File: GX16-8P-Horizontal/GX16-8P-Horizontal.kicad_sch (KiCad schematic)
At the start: 2 parts, among them J1 GX16, J2 Board Header

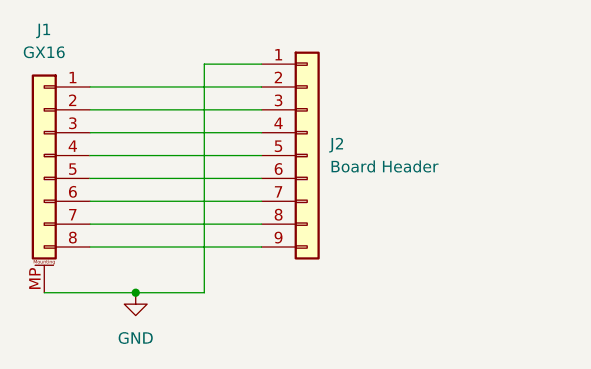
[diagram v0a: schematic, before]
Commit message: https://github.com/Halibut-Electronics/HHI-Radio-Pro/issues/34 Switched from pins to card edge.
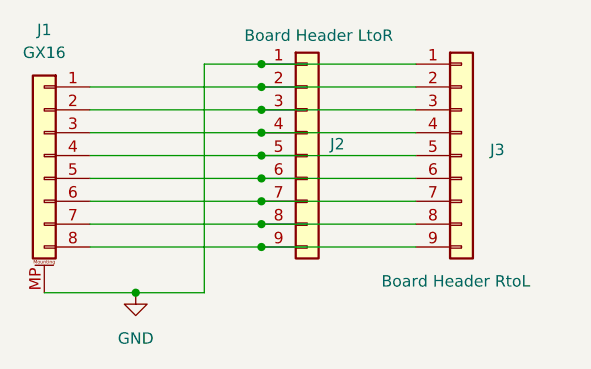
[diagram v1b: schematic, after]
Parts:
- added J3: Board Header RtoL, Libraries:Conn_B2B-RA_2.54mm_ThroughPads_9pin_RtoL, symbol Connector_Generic:Conn_01x09
- J2: value Board Header -> Board Header LtoR; footprint Connector_PinHeader_2.54mm:PinHeader_1x09_P2.54mm_Vertical -> Libraries:Conn_B2B-RA_2.54mm_ThroughPads_9pin_LtoR
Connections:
- net GND: now also J3.1 (Pin_1)
- net at J1.1 (Pin_1), J2.2 (Pin_2): now also J3.2 (Pin_2)
- net at J1.2 (Pin_2), J2.3 (Pin_3): now also J3.3 (Pin_3)
- net at J1.3 (Pin_3), J2.4 (Pin_4): now also J3.4 (Pin_4)
- net at J1.4 (Pin_4), J2.5 (Pin_5): now also J3.5 (Pin_5)
- net at J1.5 (Pin_5), J2.6 (Pin_6): now also J3.6 (Pin_6)
- net at J1.6 (Pin_6), J2.7 (Pin_7): now also J3.7 (Pin_7)
- net at J1.7 (Pin_7), J2.8 (Pin_8): now also J3.8 (Pin_8)
- net at J1.8 (Pin_8), J2.9 (Pin_9): now also J3.9 (Pin_9)
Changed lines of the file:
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@@
-(kicad_sch (version 20211123) (generator eeschema)
+(kicad_sch (version 20230121) (generator eeschema)
   (paper "A4")
+  (junction (at 127 76.2) (diameter 0) (color 0 0 0 0)
+  )
+  (junction (at 127 73.66) (diameter 0) (color 0 0 0 0)
+  )
+  (junction (at 127 83.82) (diameter 0) (color 0 0 0 0)
+  )
+  (junction (at 127 86.36) (diameter 0) (color 0 0 0 0)
+  )
+  (junction (at 127 91.44) (diameter 0) (color 0 0 0 0)
+  )
   (junction (at 113.03 99.06) (diameter 0) (color 0 0 0 0)
   )
+  (junction (at 127 88.9) (diameter 0) (color 0 0 0 0)
+  )
+  (junction (at 127 78.74) (diameter 0) (color 0 0 0 0)
+  )
+  (junction (at 127 93.98) (diameter 0) (color 0 0 0 0)
+  )
+  (junction (at 127 81.28) (diameter 0) (color 0 0 0 0)
+  )
+  (wire (pts (xy 127 91.44) (xy 144.145 91.44))
+    (stroke (width 0) (type default))
+  )
   (wire (pts (xy 107.95 91.44) (xy 127 91.44))
-    (stroke (width 0) (type default) (color 0 0 0 0))
+    (stroke (width 0) (type default))
   )
   (wire (pts (xy 120.65 73.66) (xy 127 73.66))
-    (stroke (width 0) (type default) (color 0 0 0 0))
+    (stroke (width 0) (type default))
   )
   (wire (pts (xy 107.95 86.36) (xy 127 86.36))
-    (stroke (width 0) (type default) (color 0 0 0 0))
+    (stroke (width 0) (type default))
   )
   (wire (pts (xy 113.03 99.06) (xy 120.65 99.06))
-    (stroke (width 0) (type default) (color 0 0 0 0))
+    (stroke (width 0) (type default))
+  )
+  (wire (pts (xy 127 81.28) (xy 144.145 81.28))
+    (stroke (width 0) (type default))
   )
   (wire (pts (xy 107.95 93.98) (xy 127 93.98))
-    (stroke (width 0) (type default) (color 0 0 0 0))
+    (stroke (width 0) (type default))
   )
   (wire (pts (xy 107.95 83.82) (xy 127 83.82))
-    (stroke (width 0) (type default) (color 0 0 0 0))
+    (stroke (width 0) (type default))
+  )
+  (wire (pts (xy 127 93.98) (xy 144.145 93.98))
+    (stroke (width 0) (type default))
+  )
+  (wire (pts (xy 127 78.74) (xy 144.145 78.74))
+    (stroke (width 0) (type default))
   )
   (wire (pts (xy 107.95 78.74) (xy 127 78.74))
-    (stroke (width 0) (type default) (color 0 0 0 0))
+    (stroke (width 0) (type default))
   )
   (wire (pts (xy 102.87 99.06) (xy 113.03 99.06))
-    (stroke (width 0) (type default) (color 0 0 0 0))
+    (stroke (width 0) (type default))
+  )
+  (wire (pts (xy 127 83.82) (xy 144.145 83.82))
+    (stroke (width 0) (type default))
+  )
+  (wire (pts (xy 127 86.36) (xy 144.145 86.36))
+    (stroke (width 0) (type default))
+  )
+  (wire (pts (xy 127 73.66) (xy 144.145 73.66))
+    (stroke (width 0) (type default))
   )
   (wire (pts (xy 107.95 88.9) (xy 127 88.9))
-    (stroke (width 0) (type default) (color 0 0 0 0))
+    (stroke (width 0) (type default))
   )
   (wire (pts (xy 107.95 81.28) (xy 127 81.28))
-    (stroke (width 0) (type default) (color 0 0 0 0))
+    (stroke (width 0) (type default))
   )
   (wire (pts (xy 107.95 76.2) (xy 127 76.2))
-    (stroke (width 0) (type default) (color 0 0 0 0))
+    (stroke (width 0) (type default))
   )
   (wire (pts (xy 120.65 99.06) (xy 120.65 73.66))
-    (stroke (width 0) (type default) (color 0 0 0 0))
+    (stroke (width 0) (type default))
+  )
+  (wire (pts (xy 127 76.2) (xy 144.145 76.2))
+    (stroke (width 0) (type default))
+  )
+  (wire (pts (xy 127 88.9) (xy 144.145 88.9))
+    (stroke (width 0) (type default))
   )
   (symbol (lib_id "Connector_Generic_MountingPin:Conn_01x08_MountingPin") (at 102.87 83.82 0) (mirror y) (unit 1)
-    (in_bom yes) (on_board yes) (fields_autoplaced)
-    (property "Reference" "J1" (id 0) (at 102.87 69.85 0))
-    (property "Value" "GX16" (id 1) (at 102.87 72.39 0))
-    (property "Footprint" "Libraries:Conn_GX16-8_8pin_Aviation" (id 2) (at 102.87 83.82 0)
-      (effects (font (size 1.27 1.27)) hide)
-    )
-    (property "Datasheet" "~" (id 3) (at 102.87 83.82 0)
+    (in_bom yes) (on_board yes) (dnp no) (fields_autoplaced)
+    (property "Reference" "J1" (at 102.87 69.85 0)
+      (effects (font (size 1.27 1.27)))
+    )
+    (property "Value" "GX16" (at 102.87 72.39 0)
+      (effects (font (size 1.27 1.27)))
+    )
+    (property "Footprint" "Libraries:Conn_GX16-8_8pin_Aviation" (at 102.87 83.82 0)
+      (effects (font (size 1.27 1.27)) hide)
+    )
+    (property "Datasheet" "~" (at 102.87 83.82 0)
       (effects (font (size 1.27 1.27)) hide)
     )
@@
     (pin "8")
     (pin "MP")
+    (instances
+      (project "GX16-8P-Horizontal"
+        (path "/40766177-b422-41a1-81e1-f70193c63cbd"
+          (reference "J1") (unit 1)
+        )
+      )
+    )
   )
   (symbol (lib_id "power:GND") (at 113.03 99.06 0) (unit 1)
-    (in_bom yes) (on_board yes) (fields_autoplaced)
-    (property "Reference" "#PWR01" (id 0) (at 113.03 105.41 0)
-      (effects (font (size 1.27 1.27)) hide)
-    )
-    (property "Value" "GND" (id 1) (at 113.03 104.14 0))
-    (property "Footprint" "" (id 2) (at 113.03 99.06 0)
-      (effects (font (size 1.27 1.27)) hide)
-    )
-    (property "Datasheet" "" (id 3) (at 113.03 99.06 0)
-      (effects (font (size 1.27 1.27)) hide)
-    )
-    (pin "1")
-  )
-  (symbol (lib_id "Connector_Generic:Conn_01x09") (at 132.08 83.82 0) (unit 1)
-    (in_bom yes) (on_board yes) (fields_autoplaced)
-    (property "Reference" "J2" (id 0) (at 134.62 82.5499 0)
-      (effects (font (size 1.27 1.27)) (justify left))
-    )
-    (property "Value" "Board Header" (id 1) (at 134.62 85.0899 0)
-      (effects (font (size 1.27 1.27)) (justify left))
-    )
-    (property "Footprint" "Connector_PinHeader_2.54mm:PinHeader_1x09_P2.54mm_Vertical" (id 2) (at 132.08 83.82 0)
-      (effects (font (size 1.27 1.27)) hide)
-    )
-    (property "Datasheet" "~" (id 3) (at 132.08 83.82 0)
+    (in_bom yes) (on_board yes) (dnp no) (fields_autoplaced)
+    (property "Reference" "#PWR01" (at 113.03 105.41 0)
+      (effects (font (size 1.27 1.27)) hide)
+    )
+    (property "Value" "GND" (at 113.03 104.14 0)
+      (effects (font (size 1.27 1.27)))
+    )
+    (property "Footprint" "" (at 113.03 99.06 0)
+      (effects (font (size 1.27 1.27)) hide)
+    )
+    (property "Datasheet" "" (at 113.03 99.06 0)
+      (effects (font (size 1.27 1.27)) hide)
+    )
+    (pin "1")
+    (instances
+      (project "GX16-8P-Horizontal"
+        (path "/40766177-b422-41a1-81e1-f70193c63cbd"
+          (reference "#PWR01") (unit 1)
+        )
+      )
+    )
+  )
+  (symbol (lib_id "Connector_Generic:Conn_01x09") (at 149.225 83.82 0) (unit 1)
+    (in_bom yes) (on_board yes) (dnp no)
+    (property "Reference" "J3" (at 152.4 83.185 0)
+      (effects (font (size 1.27 1.27)) (justify left))
+    )
+    (property "Value" "Board Header RtoL" (at 140.335 97.79 0)
+      (effects (font (size 1.27 1.27)) (justify left))
+    )
+    (property "Footprint" "Libraries:Conn_B2B-RA_2.54mm_ThroughPads_9pin_RtoL" (at 149.225 83.82 0)
+      (effects (font (size 1.27 1.27)) hide)
+    )
+    (property "Datasheet" "~" (at 149.225 83.82 0)
       (effects (font (size 1.27 1.27)) hide)
     )
@@
     (pin "8")
     (pin "9")
+    (instances
+      (project "GX16-8P-Horizontal"
+        (path "/40766177-b422-41a1-81e1-f70193c63cbd"
+          (reference "J3") (unit 1)
+        )
+      )
+    )
+  )
+  (symbol (lib_id "Connector_Generic:Conn_01x09") (at 132.08 83.82 0) (unit 1)
+    (in_bom yes) (on_board yes) (dnp no)
+    (property "Reference" "J2" (at 134.62 82.5499 0)
+      (effects (font (size 1.27 1.27)) (justify left))
+    )
+    (property "Value" "Board Header LtoR" (at 125.095 70.485 0)
+      (effects (font (size 1.27 1.27)) (justify left))
+    )
+    (property "Footprint" "Libraries:Conn_B2B-RA_2.54mm_ThroughPads_9pin_LtoR" (at 132.08 83.82 0)
+      (effects (font (size 1.27 1.27)) hide)
+    )
+    (property "Datasheet" "~" (at 132.08 83.82 0)
+      (effects (font (size 1.27 1.27)) hide)
+    )
+    (pin "1")
+    (pin "2")
+    (pin "3")
+    (pin "4")
+    (pin "5")
+    (pin "6")
+    (pin "7")
+    (pin "8")
+    (pin "9")
+    (instances
+      (project "GX16-8P-Horizontal"
+        (path "/40766177-b422-41a1-81e1-f70193c63cbd"
+          (reference "J2") (unit 1)
+        )
+      )
+    )
   )
   (sheet_instances
     (path "/" (page "1"))
   )
-  (symbol_instances
-    (path "/6b0d7141-ab3f-4a87-a24b-a2c211da2bd1"
-      (reference "#PWR01") (unit 1) (value "GND") (footprint "")
-    )
-    (path "/5aedc1b2-bb3a-4a28-8cc0-330f47fb6a76"
-      (reference "J1") (unit 1) (value "GX16") (footprint "Libraries:Conn_GX16-8_8pin_Aviation")
-    )
-    (path "/eca6089c-b7ec-4cae-a56d-2ce3b36397d2"
-      (reference "J2") (unit 1) (value "Board Header") (footprint "Connector_PinHeader_2.54mm:PinHeader_1x09_P2.54mm_Vertical")
-    )
-  )
 )

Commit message: https://github.com/Halibut-Electronics/HHI-Radio-Pro/issues/42 As sent to Synergetics
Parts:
- J1: Manufacturer (none) -> Renhotec Group; Or Generic (none) -> No; Part Number (none) -> GX16-F-8P
- J2, J3: now left out of the parts list
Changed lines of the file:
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@@
+      (effects (font (size 1.27 1.27)) hide)
+    )
+    (property "Manufacturer" "Renhotec Group" (at 102.87 83.82 0)
+      (effects (font (size 1.27 1.27)) hide)
+    )
+    (property "Part Number" "GX16-F-8P" (at 102.87 83.82 0)
+      (effects (font (size 1.27 1.27)) hide)
+    )
+    (property "Or Generic" "No" (at 102.87 83.82 0)
       (effects (font (size 1.27 1.27)) hide)
     )
@@
   )
   (symbol (lib_id "Connector_Generic:Conn_01x09") (at 149.225 83.82 0) (unit 1)
-    (in_bom yes) (on_board yes) (dnp no)
+    (in_bom no) (on_board yes) (dnp no)
     (property "Reference" "J3" (at 152.4 83.185 0)
       (effects (font (size 1.27 1.27)) (justify left))
@@
   )
   (symbol (lib_id "Connector_Generic:Conn_01x09") (at 132.08 83.82 0) (unit 1)
-    (in_bom yes) (on_board yes) (dnp no)
+    (in_bom no) (on_board yes) (dnp no)
     (property "Reference" "J2" (at 134.62 82.5499 0)
       (effects (font (size 1.27 1.27)) (justify left))
